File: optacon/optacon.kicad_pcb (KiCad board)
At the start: 2 copper layers, 31.7 x 90.2 mm, 37 parts, among them J1 Conn_01x12, J2 Conn_01x40_Socket, U1 HV528, U2 HV528, U3 DRV2665

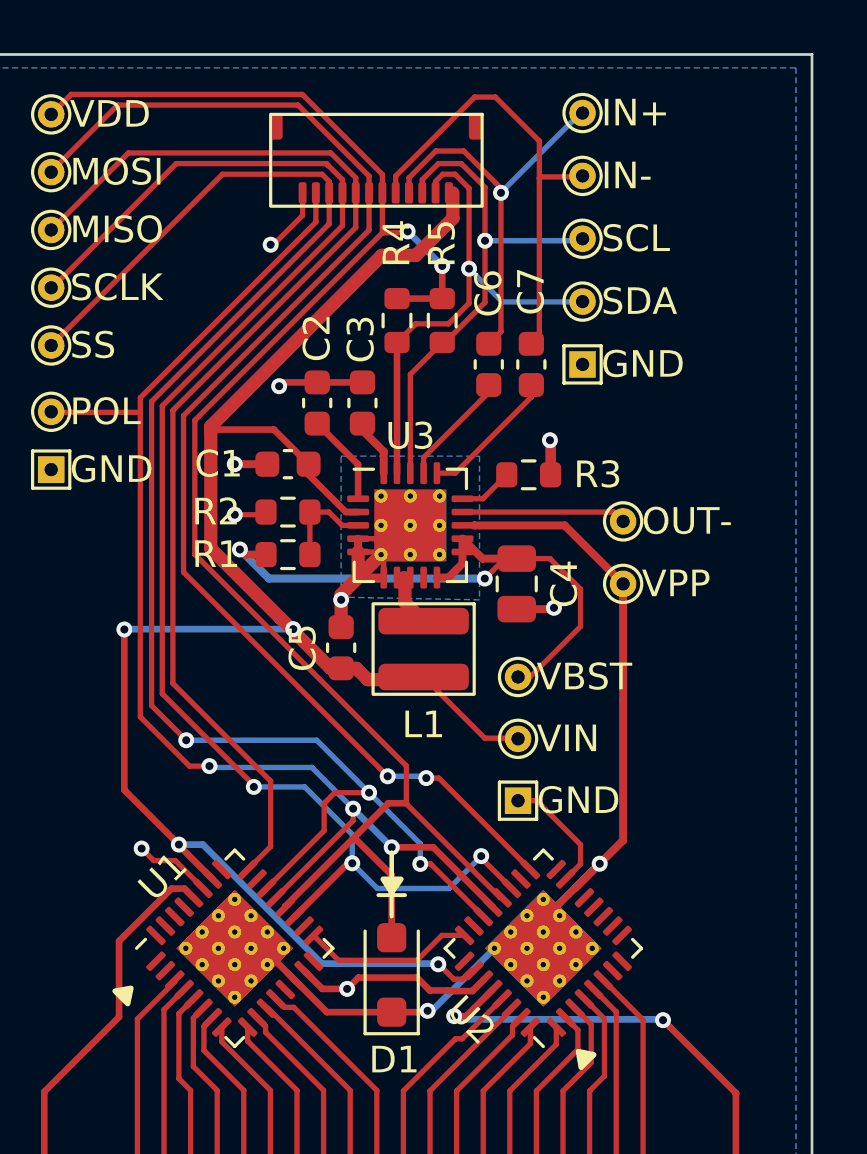
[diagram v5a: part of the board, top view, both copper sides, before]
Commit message: move SDA trace around R4, R5
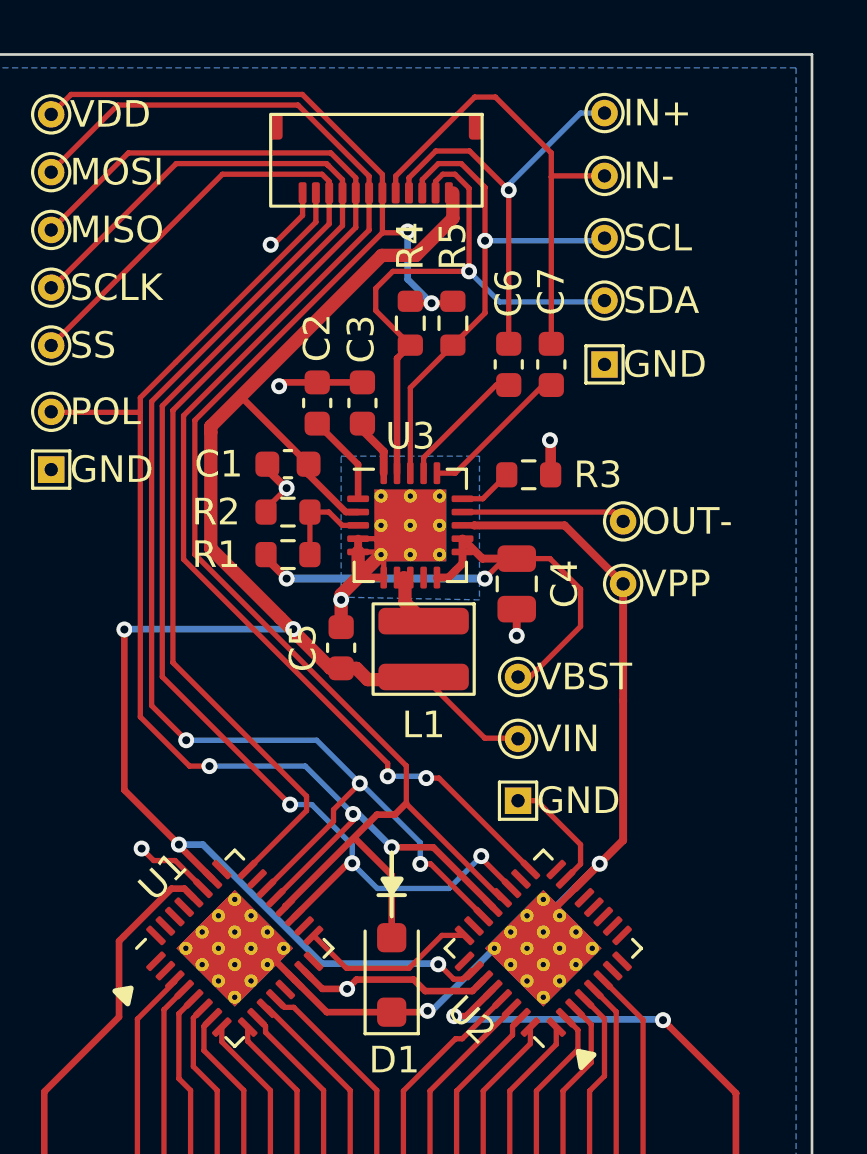
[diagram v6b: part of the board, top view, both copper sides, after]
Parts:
- moved TP10 0.83 mm to (112.2, 49.6)
- moved TP11 0.83 mm to (112.2, 47.3)
- moved TP2 0.83 mm to (112.2, 52.0)
- moved TP6 0.83 mm to (112.2, 42.6)
- moved TP7 0.83 mm to (112.2, 45.0)
- moved C6 0.75 mm to (108.6, 52.0)
- moved C7 0.75 mm to (110.2, 52.0)
- moved R4 0.51 mm to (104.9, 50.5)
- moved R5 0.41 mm to (106.5, 50.5)
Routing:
- net /SDA: track 19.4 -> 22.2 mm
- net /VBST: track 24.1 -> 22.1 mm
- net /MISO: track 43.8 -> 44.9 mm
- net /VIN: track 70.7 -> 69.9 mm
- net /SCL: track 19.0 -> 19.8 mm
- net /IN+: track 15.3 -> 16.0 mm
- net /SCLK: track 56.3 -> 55.6 mm
- net Net-(U3-IN+): track 4.33 -> 4.92 mm
- net /SS: track 57.8 -> 57.3 mm
- net /IN-: track 17.3 -> 17.8 mm
- net GND: track 35.4 -> 35.1 mm, vias 9 -> 8

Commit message: work in progress: reorder project files
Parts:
- moved TP14 0.46 mm to (91.4, 51.8)
- moved TP2 0.40 mm to (91.4, 56.4)
- moved TP12 0.33 mm to (91.4, 49.5)
- moved TP13 0.27 mm to (91.4, 54.1)
- moved TP9 0.21 mm to (91.4, 47.2)
- moved TP8 0.08 mm to (91.4, 44.9)
